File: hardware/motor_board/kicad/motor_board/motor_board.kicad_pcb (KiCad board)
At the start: 4 copper layers, 85 x 35 mm, 232 parts, among them J1 BOOMELE_1.27-2x10P, J2 BM06B-SRSS-TB, J3 BM06B-SRSS-TB, J4 B5B-XH-A, Q1 HYG015N04LS1C2, Q2 HYG015N04LS1C2, Q3 HYG015N04LS1C2, Q4 HYG015N04LS1C2, Q5 HYG015N04LS1C2, Q6 HYG015N04LS1C2, Q7 HYG015N04LS1C2, Q8 HYG015N04LS1C2, U1 STM32G474RET6, U10 SN74LVC3G17DCUR, U11 TPS22945DCKR, U12 TPS22945DCKR, U13 LM74502DDFR, U14 74LVC1G17SE-7, U2 DRV8323RHRGZR, U3 DRV8316CRRGFR, U4 DRV8316CRRGFR, U5 AP2112K-3.3TRG1, U6 SN74LVC08ABQAR, U7 INA239AIDGSR, U8 BQ76907RGRR, U9 SN74LVC3G17DCUR

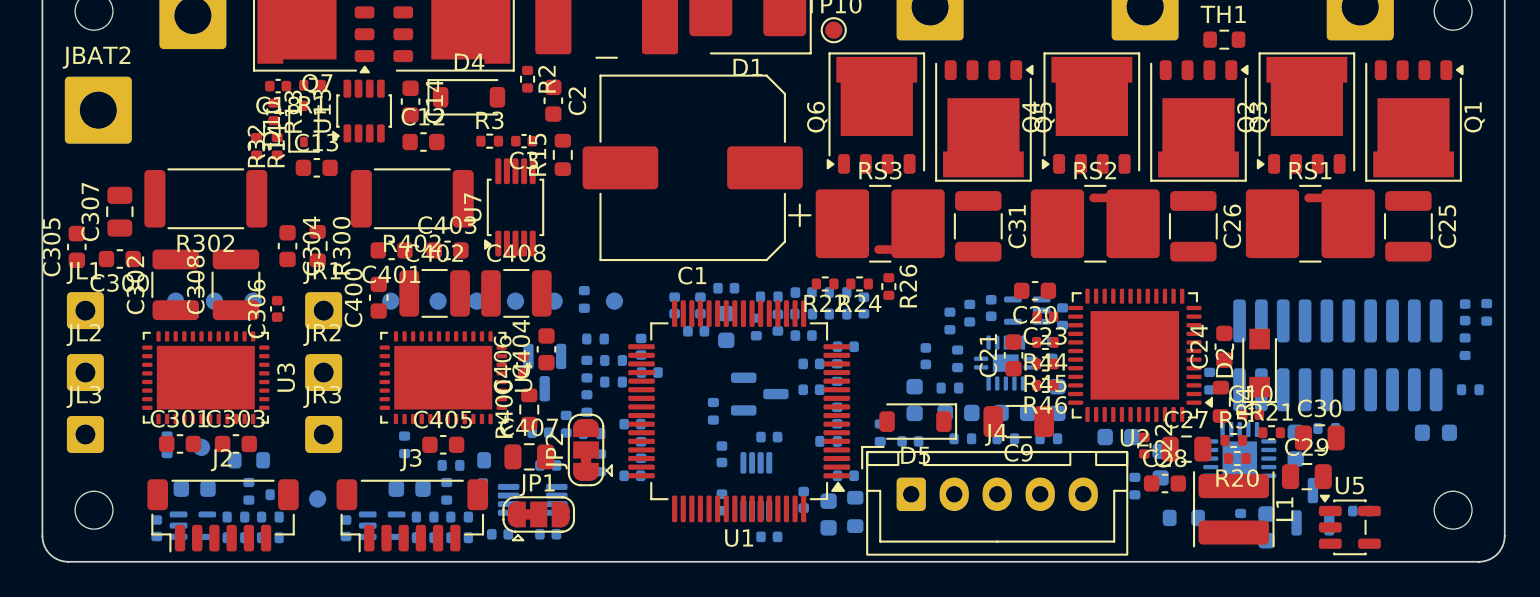
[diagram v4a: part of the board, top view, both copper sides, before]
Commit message: Rev L3: MCU pin map co-assigned with the v2 placement (kicad/v2/pinsolve.py, CP-SAT on the real pads): architecture unchanged (TIM1 weapon, TIM8/TIM20 drives, TIM3/TIM2 sensors, ADC5 drive L, ADC3/4 drive R, SPI3, USART1); break inputs on BKIN only, one port per EXTI line, motor-NTC inputs on 5 V-tolerant pins, PB8-BOOT0 on a pulled-up chip select; DESIGN 3.x/7/8/9 and CHANGES updated (ADC ranks re-derived); schematic regenerated (176/176), board rebuilt and re-placed (U4 rotated, JR on the rear edge, J3 + sensor R front end at the rear-right); global router (groute.py, gate.py, gstats.py) with v1 calibration; Freerouting trial script
Co-Authored-By: Claude Opus 5.5 (1M context) <noreply@anthropic.com>
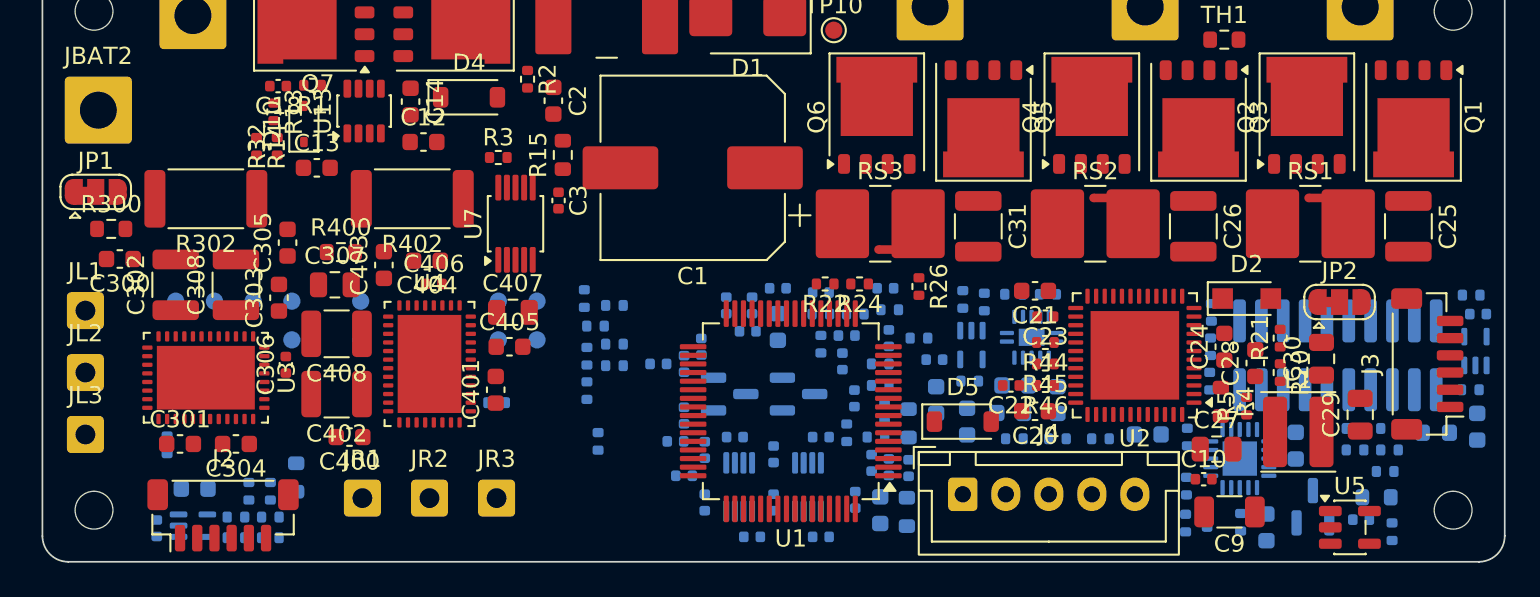
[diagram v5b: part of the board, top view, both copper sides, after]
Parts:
- moved C49 67.0 mm to (183.4, 90.6), turned to 180 degrees
- moved U12 64.4 mm to (183.3, 92.8), turned to 90 degrees
- moved C48 62.2 mm to (183.4, 97.2), turned to -90 degrees
- moved R114 62.2 mm to (183.1, 89.5)
- moved J3 59.7 mm to (180.5, 93.5), turned to 90 degrees
- moved R57 56.4 mm to (178.3, 97.2), turned to 180 degrees
- moved R116 54.3 mm to (178.1, 99.8), turned to 180 degrees
- moved R58 54.3 mm to (178.3, 98.5), turned to 180 degrees
- moved R59 52.9 mm to (176.3, 98.5), turned to 180 degrees
- moved R115 52.3 mm to (176.3, 97.2), turned to 180 degrees
- moved R117 51.1 mm to (177.6, 101.2), turned to 180 degrees
- moved JP2 44.6 mm to (175.4, 89.9), turned to 0 degrees
- moved C73 39.1 mm to (167.7, 102.5), turned to -90 degrees
- moved R53 36.5 mm to (166.4, 102.8), turned to 90 degrees
- moved JP1 31.9 mm to (103.1, 83.5)
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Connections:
- U1 pad 11: /mcu/L_SOC_F -> W_VC
- U1 pad 13: W_SOB -> W_SOC
- U1 pad 14: W_VC -> /mcu/VBAT_SNS
- U1 pad 17: /mcu/VBAT_SNS -> W_SOB
- U1 pad 18: W_VA -> W_NTC
- U1 pad 2: W_nFAULT -> unconnected-(U1-PC13-Pad2)
- U1 pad 20: W_NTC -> W_nFAULT
- U1 pad 21: W_INLA_M -> W_INLC_M
- U1 pad 22: /mcu/MB_TX -> W_VA
- U1 pad 23: /mcu/MB_RX -> INA_nCS
- U1 pad 25: /mcu/R_SOC_F -> /mcu/R_SOA_F
- U1 pad 26: R_INHA -> R_INHC
- U1 pad 3: DRV_OFF -> W_EN
- U1 pad 33: W_SOC -> R_nCS
- U1 pad 34: /mcu/R_SOA_F -> /mcu/R_SOB_F
- U1 pad 35: /mcu/R_SOB_F -> /mcu/R_SOC_F
- U1 pad 36: W_INLB_M -> /mcu/L_SOA_F
- U1 pad 37: W_INLC_M -> W_INLA_M
- U1 pad 38: unconnected-(U1-PC6-Pad38) -> L_INHA
- U1 pad 4: R_nFAULT -> W_ARM_S
- U1 pad 40: R_INHC -> R_INHA
- U1 pad 41: L_nCS -> R_nFAULT
- U1 pad 42: /mcu/L_SOA_F -> /mcu/L_SOB_F
- U1 pad 43: /mcu/L_SOB_F -> /mcu/L_SOC_F
- U1 pad 44: W_INHC -> W_INHA
- U1 pad 45: R_nCS -> DRV_OFF
- U1 pad 46: W_EN -> W_INLB_M
- U1 pad 5: L_MTEMP -> R_MTEMP
- U1 pad 55: W_ARM_S -> L_nFAULT
- U1 pad 59: L_INHA -> /mcu/MB_TX
- U1 pad 6: R_MTEMP -> L_MTEMP
- U1 pad 60: L_nFAULT -> /mcu/MB_RX
- U1 pad 61: INA_nCS -> L_nCS
- U1 pad 8: W_INHA -> W_INHC

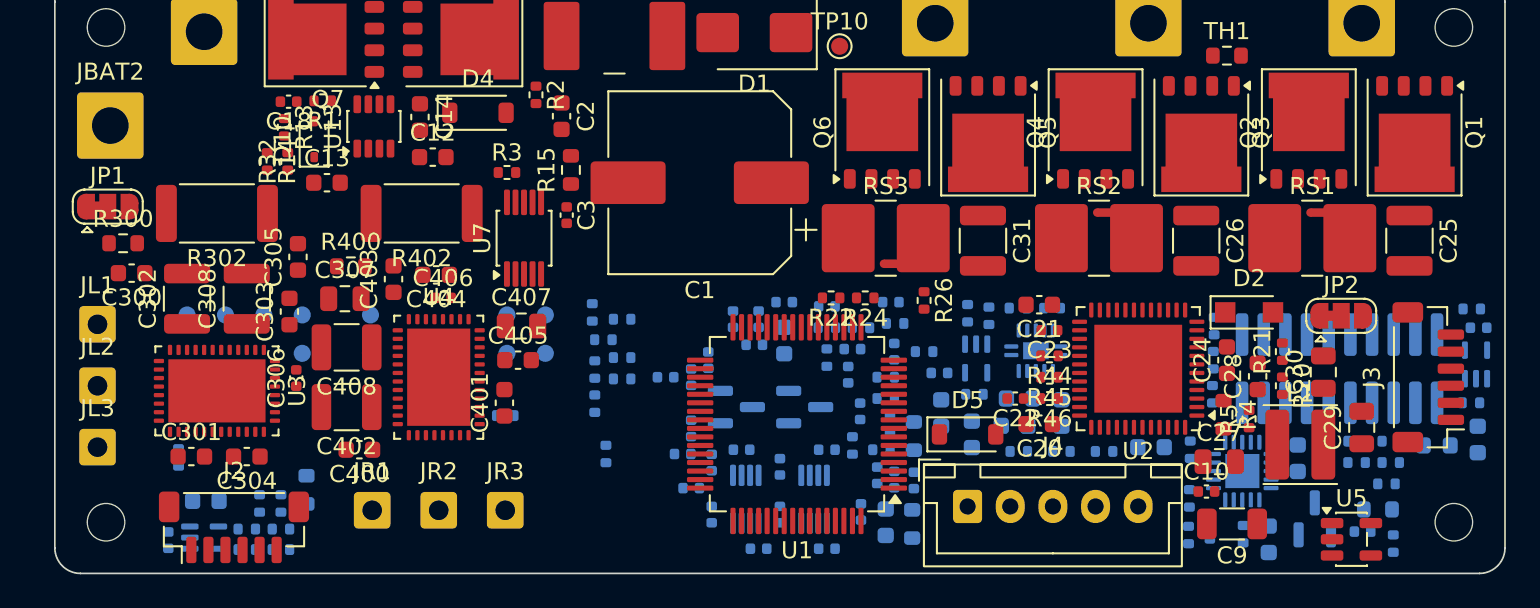
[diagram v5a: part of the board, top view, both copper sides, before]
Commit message: v2 placement round 2: DRV8316/DRV8323 decoupling anchored to the exact pins it serves and placed first, fan-out keep-outs at the U2/U3/U4 pin rows and a ring around the MCU, L4 corridor under the drive-to-MCU path kept free of bottom parts, test pads on the top, MCU at x 38 and J4 behind the MCU/U2 gap so the buck sits at U2's rear-right corner. Freerouting trial: 77 -> 53 signal/rail opens on round 1's fixes
Co-Authored-By: Claude Opus 5.5 (1M context) <noreply@anthropic.com>
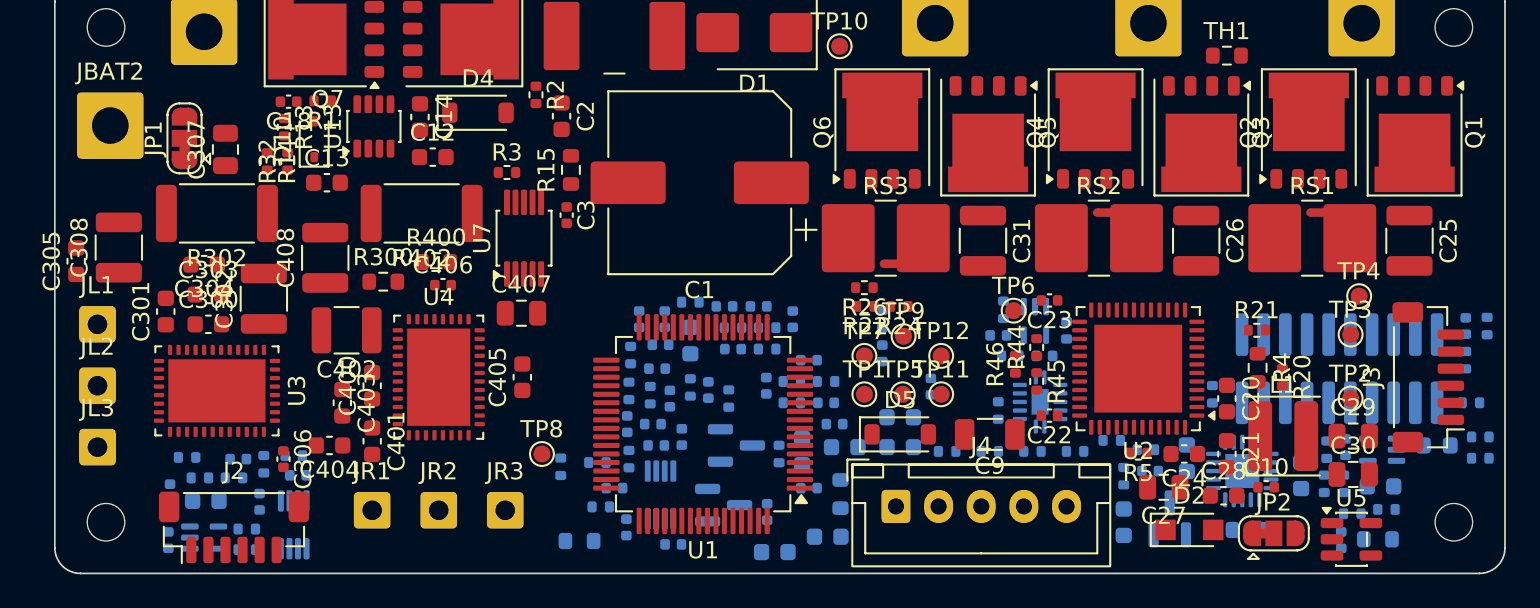
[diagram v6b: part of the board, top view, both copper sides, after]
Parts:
- TP1, TP11, TP12, TP2, TP3, TP4, TP5, TP6, TP7, TP8, TP9: moved to F.Cu
- moved TP3 68.2 mm to (175.9, 91.0)
- moved TP2 63.9 mm to (175.9, 94.8)
- moved TP4 62.0 mm to (176.4, 88.8)
- moved C112 38.6 mm to (106.8, 100.2), turned to 90 degrees
- moved TP1 37.7 mm to (147.4, 94.5)
- moved TP5 35.3 mm to (149.7, 94.5)
- moved C111 34.5 mm to (110.8, 98.3), turned to 180 degrees
- moved TP11 33.5 mm to (151.9, 94.5)
- moved C110 30.6 mm to (112.0, 100.8)
- moved U9 30.5 mm to (114.0, 102.2), turned to 90 degrees
- moved TP6 29.7 mm to (156.2, 89.6)
- moved C47 28.3 mm to (114.2, 99.2), turned to 180 degrees
- moved TP12 23.2 mm to (151.9, 92.2)
- moved TP9 21.0 mm to (149.8, 91.1)
- moved TP7 21.0 mm to (147.4, 92.2)
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
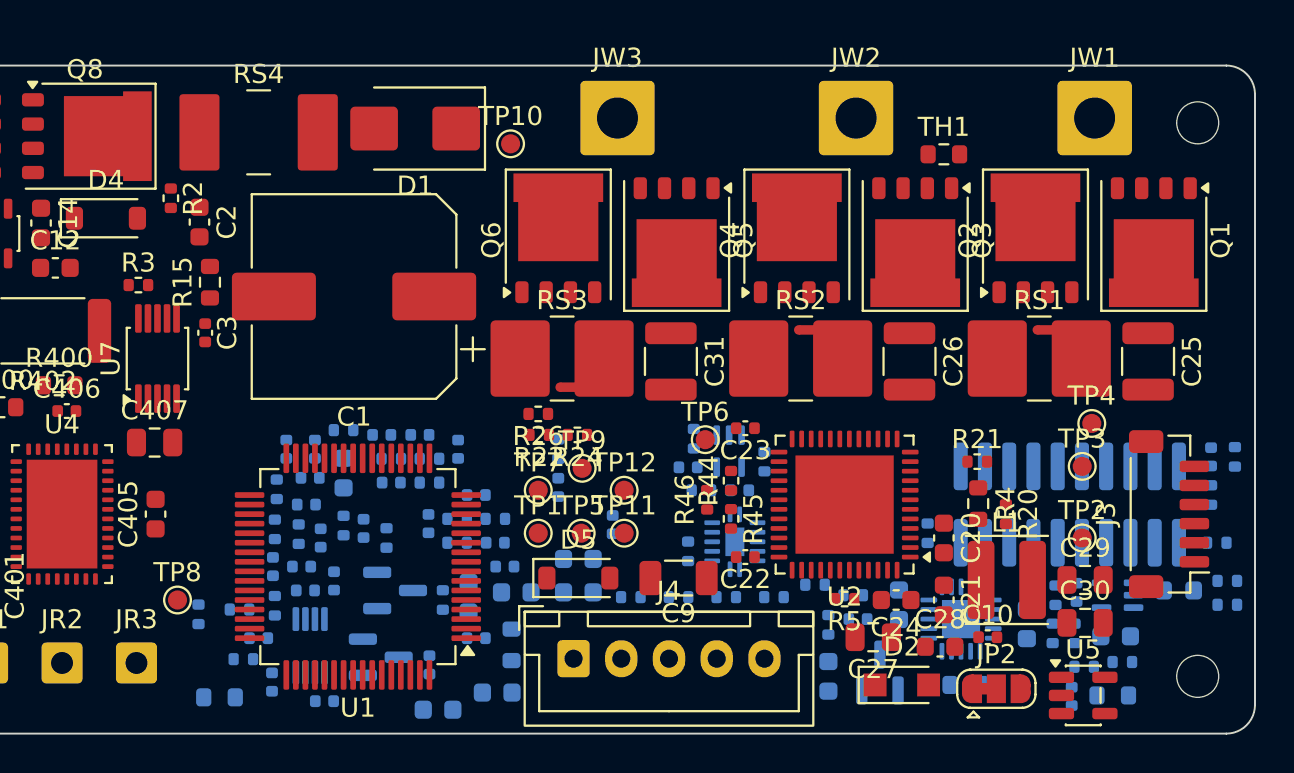
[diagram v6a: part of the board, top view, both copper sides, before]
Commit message: v2 bridge gate/Kelvin pre-route (gate-corridor option 3, decided 2026-09-30): HS gate pairs in short L4 lanes under the cells, LS gates on L1 through the shunt gaps with no via, Kelvin via L4 hops; cells B/A +0.6 mm, U2 to y 24.0, net ties at the gap rear; 12 POFV vias (U2 pins 13/14/18/19/21-24, RS2 SL, NT1-3 SN); experiment board DRC 0 errors (kicad/gen/v2_bridge.py, kicad/v2/README_bridge.md)
Co-Authored-By: Claude Opus 5.5 (1M context) <noreply@anthropic.com>
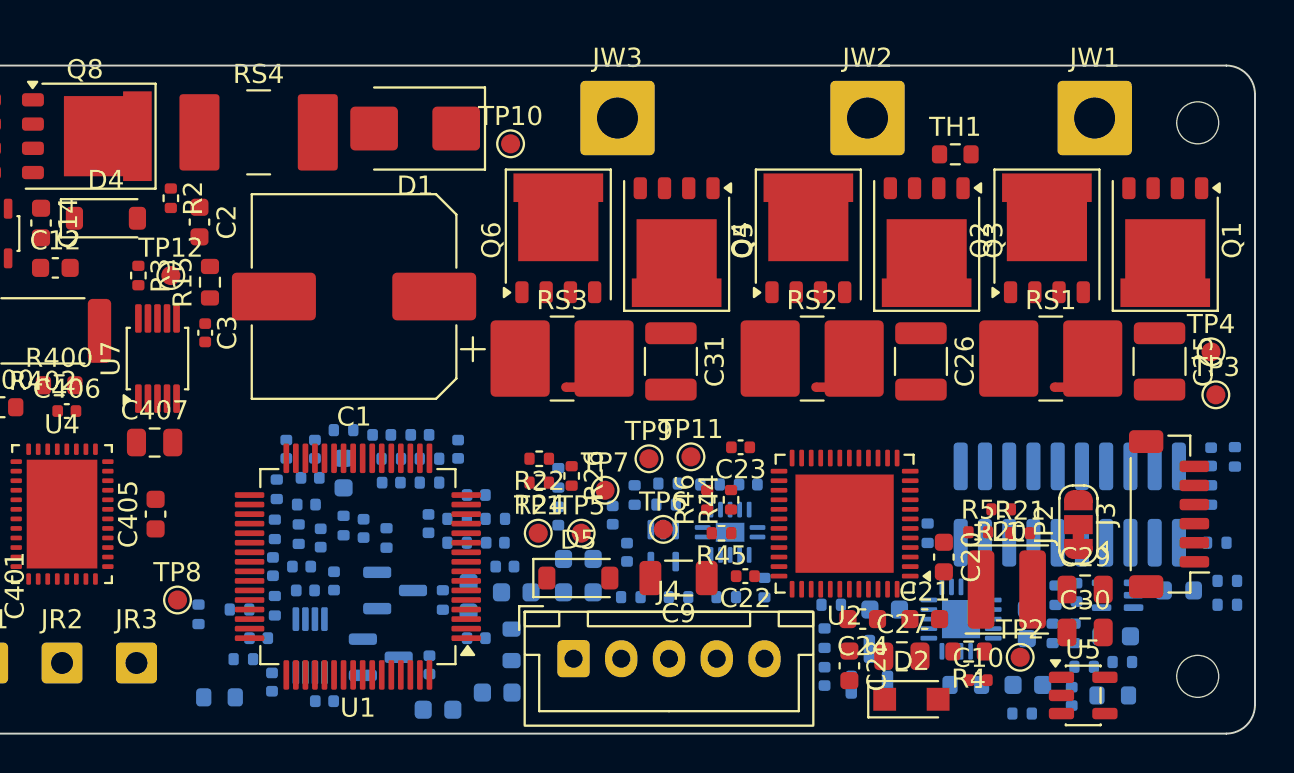
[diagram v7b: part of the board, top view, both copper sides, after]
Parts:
- moved TP12 26.3 mm to (128.2, 81.0)
- moved R41 11.2 mm to (172.8, 104.0), turned to 0 degrees
- moved C16 10.5 mm to (173.1, 102.5), turned to 0 degrees
- moved JP2 9.62 mm to (175.8, 94.0), turned to 90 degrees
- moved R48 9.35 mm to (154.2, 91.9), turned to 180 degrees
- moved R40 8.28 mm to (162.8, 98.2), turned to 0 degrees
- moved TP3 7.94 mm to (182.9, 87.2)
- moved R5 7.83 mm to (170.5, 94.5), turned to 0 degrees
- moved R4 7.77 mm to (170.0, 100.7), turned to 180 degrees
- moved TP4 7.29 mm to (182.7, 85.0)
- moved TP2 7.04 mm to (172.7, 101.0)
- moved U14 6.03 mm to (154.0, 95.2)
- moved C17 5.48 mm to (152.1, 95.5), turned to 90 degrees
- moved TP11 5.32 mm to (155.4, 90.5)
- moved TP6 5.19 mm to (154.0, 94.3)
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
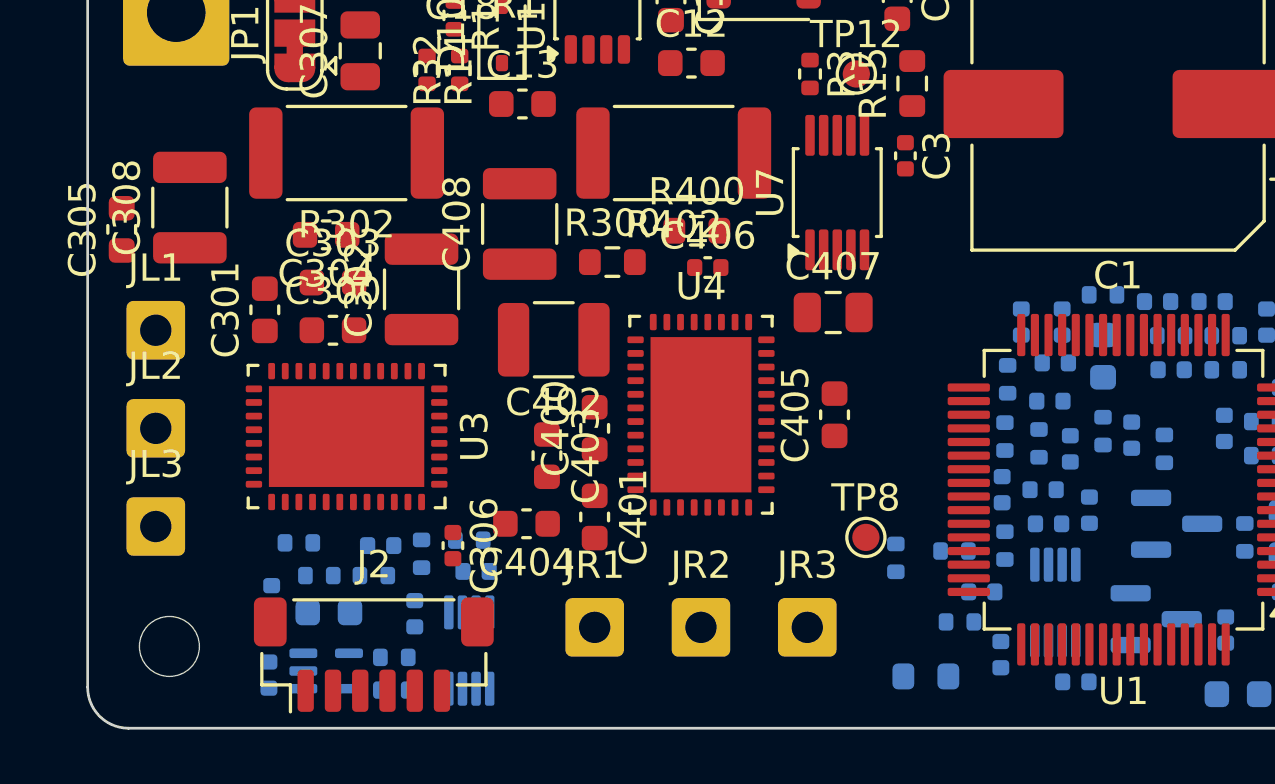
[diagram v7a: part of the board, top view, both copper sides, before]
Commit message: v2 drive fan-out pre-route (kicad/gen/v2_drive.py on top of v2_bridge): every U3/U4 net connected to its decoupling, the MCU and the CSA filters, DRC 0; placement moves (R300/R400 swapped, R401, R81, R82, C305); L3 VBAT edge y = 16.0 also for x 14-27 (DESIGN 6.2); 4 more POFV (U1.42, U1.45, U4.5, U4.37); fr_trial island rule areas tracks-only
Co-Authored-By: Claude Opus 5.5 (1M context) <noreply@anthropic.com>
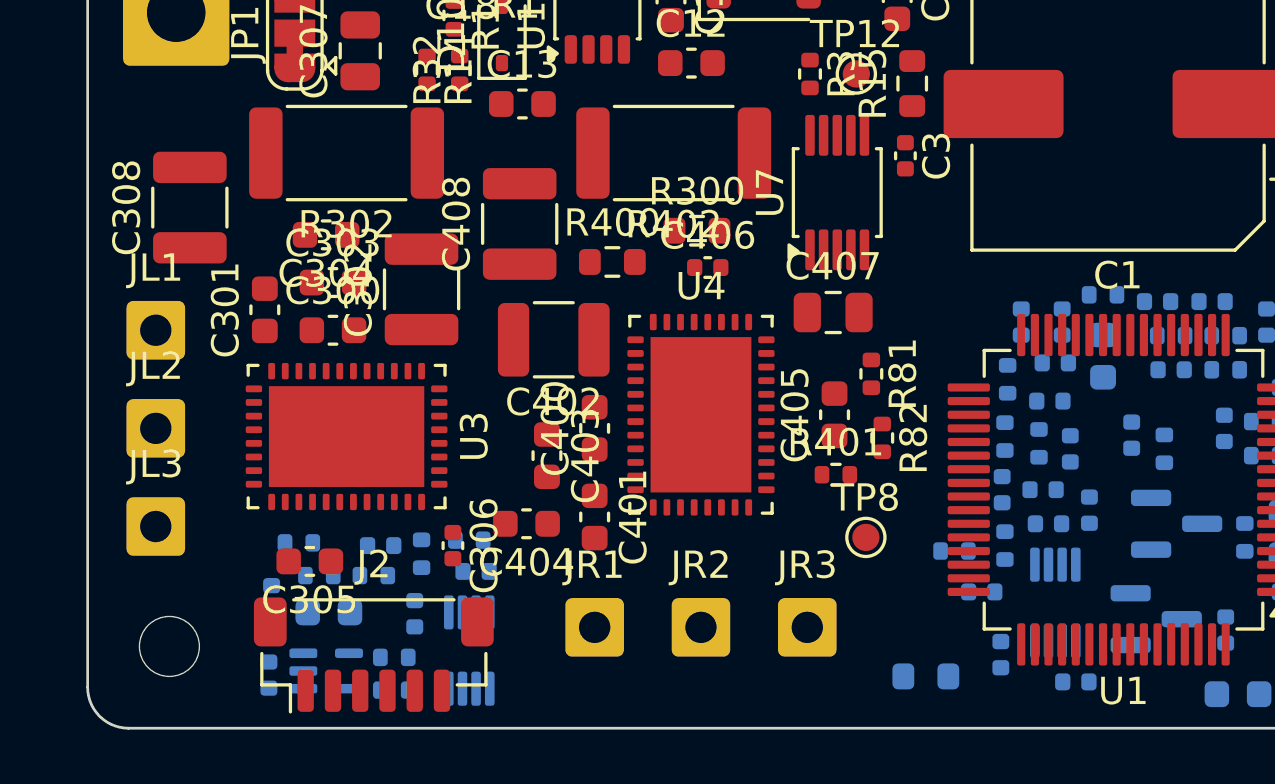
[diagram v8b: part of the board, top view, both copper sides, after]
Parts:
- R401, R81, R82: moved to F.Cu
- moved C305 14.0 mm to (108.2, 98.9), turned to 180 degrees
- moved R81 9.66 mm to (128.8, 92.0), turned to -90 degrees
- moved R82 8.10 mm to (129.2, 94.3)
- moved R401 3.76 mm to (127.5, 95.7), turned to 0 degrees
- moved R300 3.31 mm to (122.4, 86.8)
- moved R400 3.30 mm to (119.2, 87.9)
